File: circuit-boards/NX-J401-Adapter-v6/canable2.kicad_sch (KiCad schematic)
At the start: 26 parts, among them J8 SWD, J9 CFG, Q6 SI2301CDS-T1-GE3, Q7 SS8050, Q8 SI2301CDS-T1-GE3, U2 RT9013-33GB, U3 STM32G431CBTx, U4 TJA1051TK-3

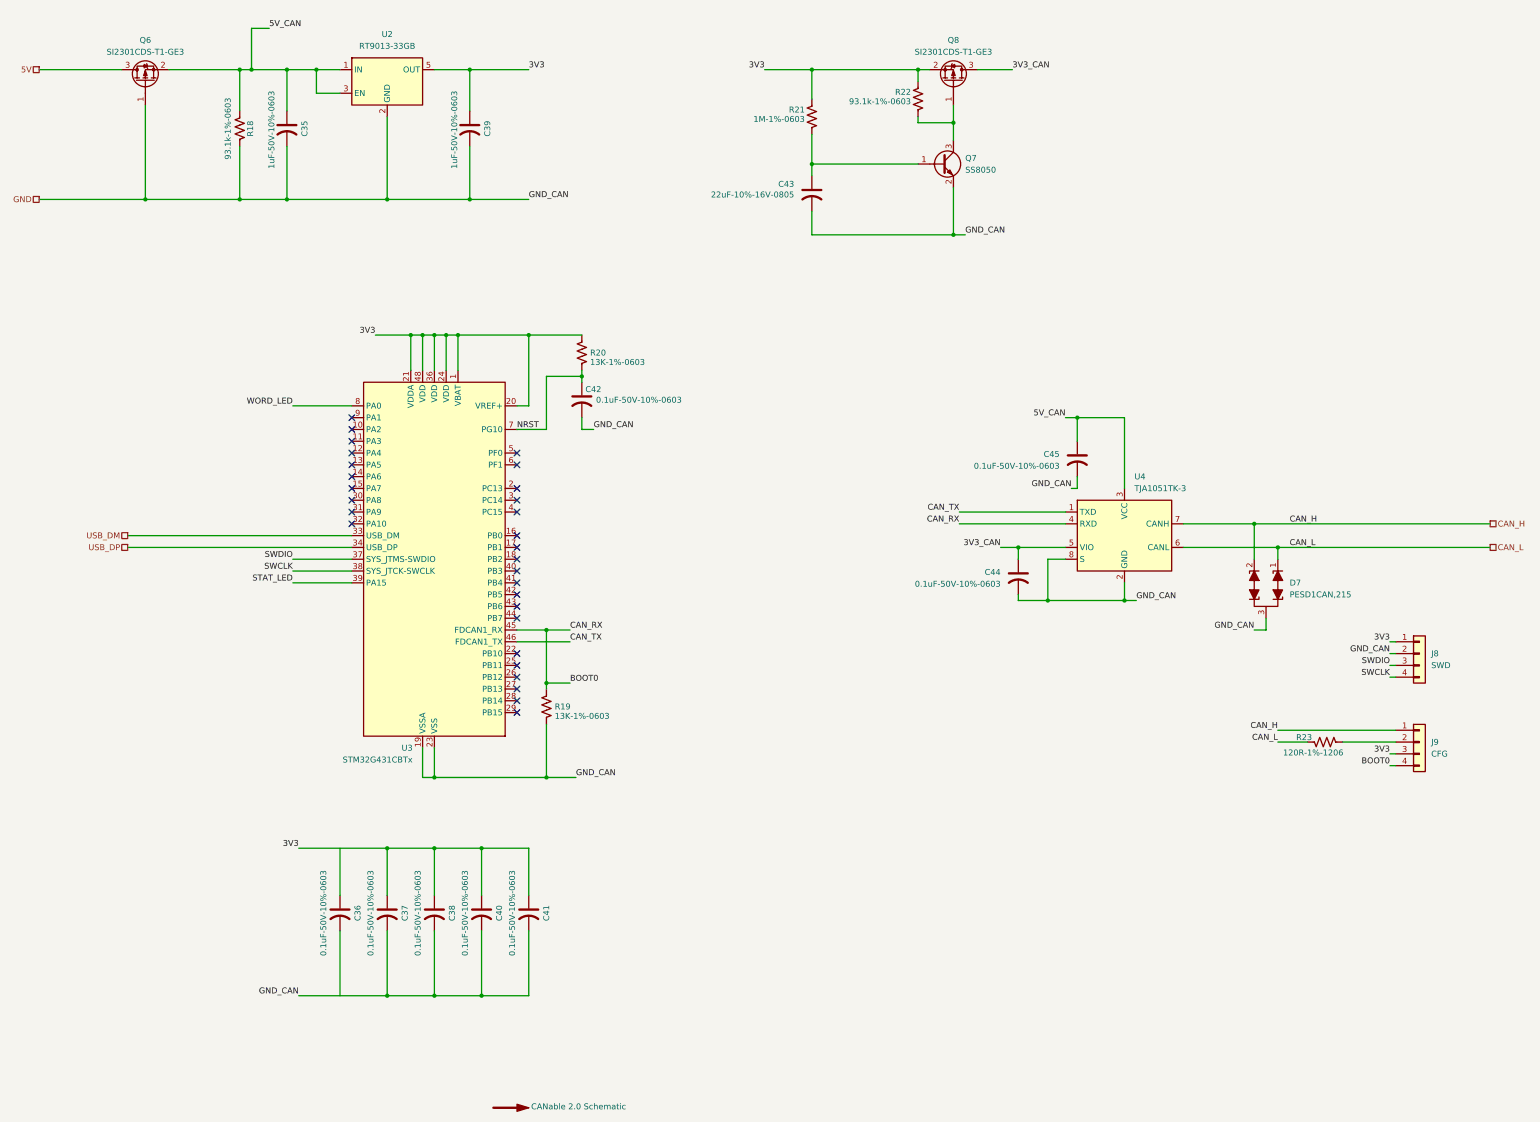
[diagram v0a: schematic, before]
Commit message: Changed canable to use 3.3V power form USB to use key-e connector that breaks out USB and 3V3
Signed-off-by: Scott Berman <sgberman1@gmail.com>
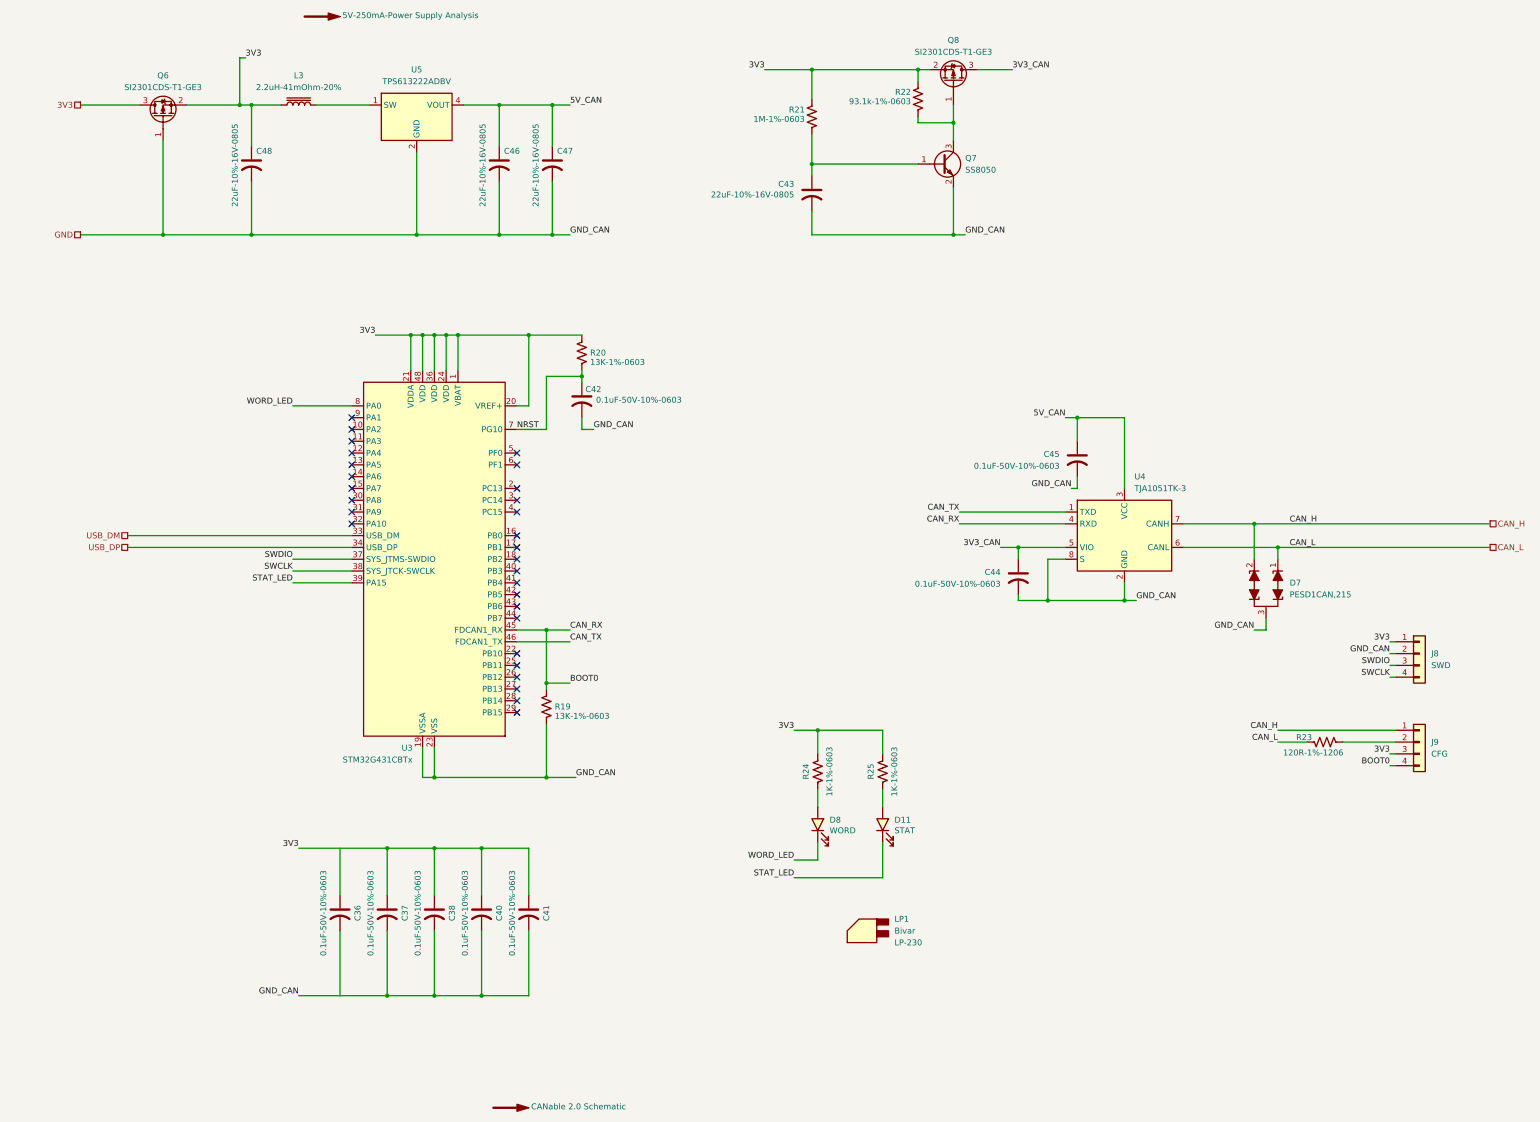
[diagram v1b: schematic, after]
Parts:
- removed C35, C39: 1uF-50V-10%-0603, Capacitor_SMD:C_0603_1608Metric, symbol Device:C_US
- removed R18: 93.1k-1%-0603, Resistor_SMD:R_0603_1608Metric, symbol Device:R_US
- removed U2: RT9013-33GB, Package_TO_SOT_SMD:SOT-23-5, symbol NX-J401-Adapter:RT9013-33GB
- added C46, C47, C48: 22uF-10%-16V-0805, Capacitor_SMD:C_0805_2012Metric, symbol Device:C_US
- added D11: STAT, LED_SMD:LED_1206_3216Metric, symbol Device:LED
- added D8: WORD, LED_SMD:LED_1206_3216Metric, symbol Device:LED
- added L3: 2.2uH-41mOhm-20%, NX-J401-Adapter:KOHER-MDA4020-2R2M, symbol Device:L_Iron
- added LP1: (no value), NX-J401-Adapter:Bivar-LP-230, symbol NX-J401-Adapter:Light_Pipe
- added R24, R25: 1K-1%-0603, Resistor_SMD:R_0603_1608Metric, symbol Device:R_US
- added U5: TPS613222ADBV, Package_TO_SOT_SMD:SOT-23-5, symbol Regulator_Switching:TPS613222ADBV
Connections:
- net 5V is gone; now on net 3V3: Q6.3 (D)
- net 3V3: now also Q6.2 (S), C48.1, L3.1, R24.1, R25.1
- net 5V_CAN: now also C46.1, C47.1, U5.4 (VOUT); no longer Q6.2 (S)
- net GND: now also C46.2, C47.2, C48.2, U5.2 (GND)
- net STAT_LED: now also D11.1 (K)
- net WORD_LED: now also D8.1 (K)
- new net: D11.2 (A), R25.2
- new net: D8.2 (A), R24.2
- new net: L3.2, U5.1 (SW)
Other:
- moved on the sheet: Q6

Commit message: WIP update
Signed-off-by: Scott Berman <sgberman1@gmail.com>
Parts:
- J8: footprint Connector_PinHeader_2.54mm:PinHeader_1x04_P2.54mm_Vertical -> Connector_PinHeader_2.54mm:PinHeader_1x04_P2.54mm_Horizontal
- J9: footprint Connector_PinHeader_2.54mm:PinHeader_2x02_P2.54mm_Vertical -> Connector_PinHeader_2.54mm:PinHeader_1x04_P2.54mm_Horizontal
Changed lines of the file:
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@@
 			)
 		)
-		(property "Footprint" "Connector_PinHeader_2.54mm:PinHeader_2x02_P2.54mm_Vertical"
+		(property "Footprint" "Connector_PinHeader_2.54mm:PinHeader_1x04_P2.54mm_Horizontal"
 			(at 346.71 177.8 0)
 			(hide yes)
@@
 			)
 		)
-		(property "Footprint" "Connector_PinHeader_2.54mm:PinHeader_1x04_P2.54mm_Vertical"
+		(property "Footprint" "Connector_PinHeader_2.54mm:PinHeader_1x04_P2.54mm_Horizontal"
 			(at 346.71 158.75 0)
 			(hide yes)

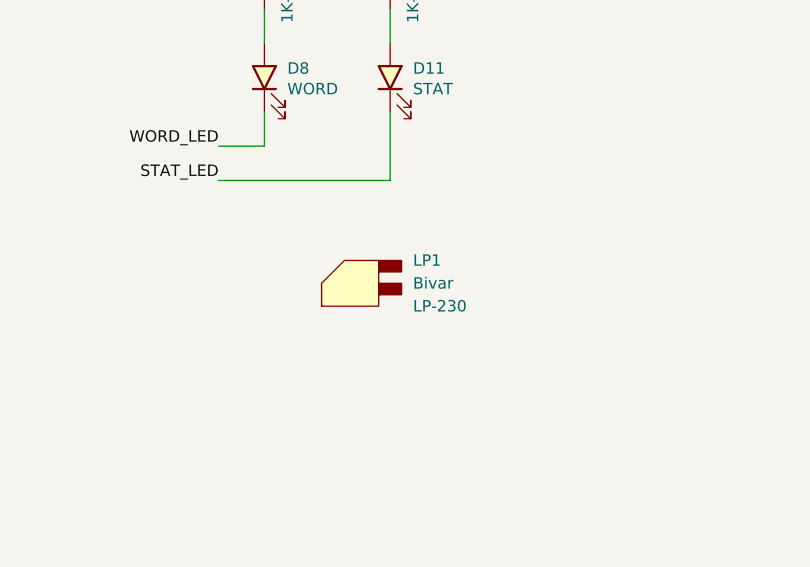
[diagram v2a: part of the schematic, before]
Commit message: Changed USB header ot pico lock and light pipe to single row
Signed-off-by: Scott Berman <sgberman1@gmail.com>
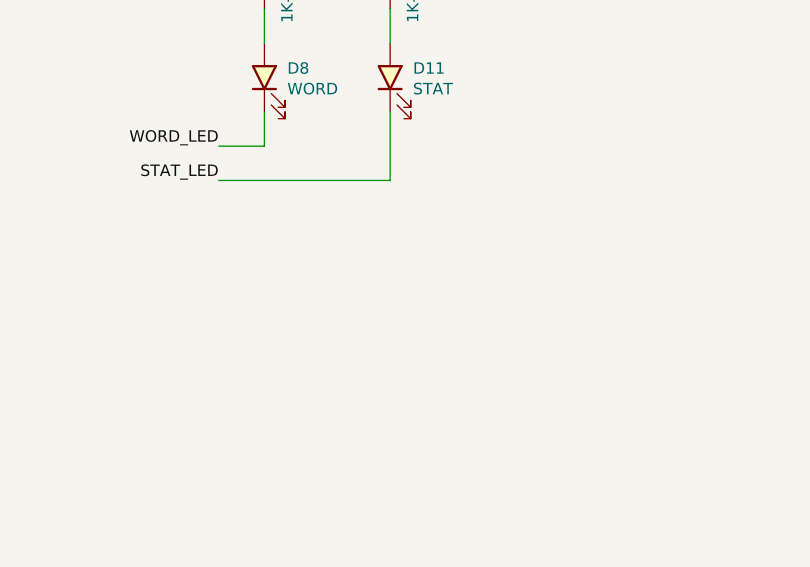
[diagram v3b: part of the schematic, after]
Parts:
- removed LP1: (no value), NX-J401-Adapter:Bivar-LP-230, symbol NX-J401-Adapter:Light_Pipe
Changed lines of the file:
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@@
-	)
-	(symbol
-		(lib_id "NX-J401-Adapter:Light_Pipe")
-		(at 223.52 218.44 0)
-		(unit 1)
-		(body_style 1)
-		(exclude_from_sim no)
-		(in_bom yes)
-		(on_board yes)
-		(in_pos_files yes)
-		(dnp no)
-		(fields_autoplaced yes)
-		(property "Reference" "LP1"
-			(at 233.68 215.8999 0)
-			(show_name no)
-			(do_not_autoplace no)
-			(effects
-				(font
-					(size 1.27 1.27)
-				)
-				(justify left)
-			)
-		)
-		(property "Value" ""
-			(at 223.52 218.44 0)
-			(show_name no)
-			(do_not_autoplace no)
-			(effects
-				(font
-					(size 1.27 1.27)
-				)
-			)
-		)
-		(property "Footprint" "NX-J401-Adapter:Bivar-LP-230"
-			(at 223.52 218.44 0)
-			(hide yes)
-			(show_name no)
-			(do_not_autoplace no)
-			(effects
-				(font
-					(size 1.27 1.27)
-				)
-			)
-		)
-		(property "Datasheet" "Components/Bivar-LP-230.pdf"
-			(at 223.52 218.44 0)
-			(hide yes)
-			(show_name no)
-			(do_not_autoplace no)
-			(effects
-				(font
-					(size 1.27 1.27)
-				)
-			)
-		)
-		(property "Description" ""
-			(at 223.52 218.44 0)
-			(hide yes)
-			(show_name no)
-			(do_not_autoplace no)
-			(effects
-				(font
-					(size 1.27 1.27)
-				)
-			)
-		)
-		(property "MFG" "Bivar"
-			(at 233.68 218.4399 0)
-			(show_name no)
-			(do_not_autoplace no)
-			(effects
-				(font
-					(size 1.27 1.27)
-				)
-				(justify left)
-			)
-		)
-		(property "MFG P/N" "LP-230"
-			(at 233.68 220.9799 0)
-			(show_name no)
-			(do_not_autoplace no)
-			(effects
-				(font
-					(size 1.27 1.27)
-				)
-				(justify left)
-			)
-		)
-		(property "DIST" "Digikey"
-			(at 223.52 218.44 0)
-			(hide yes)
-			(show_name no)
-			(do_not_autoplace no)
-			(effects
-				(font
-					(size 1.27 1.27)
-				)
-			)
-		)
-		(property "DIST P/N" "492-1859-ND"
-			(at 223.52 218.44 0)
-			(hide yes)
-			(show_name no)
-			(do_not_autoplace no)
-			(effects
-				(font
-					(size 1.27 1.27)
-				)
-			)
-		)
-		(instances
-			(project "NX-J401-Adapter-v6"
-				(path "/3c9fa76f-2b37-4666-8575-58caa65def04/958ef65b-dc3d-4755-b7b0-3d4dc8feed9f"
-					(reference "LP1")
-					(unit 1)
-				)
-			)
-		)
 	)
 	(symbol

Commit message: Improved placement.  Pre-routing
Signed-off-by: Scott Berman <sgberman1@gmail.com>
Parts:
- removed J8: SWD, Connector_PinHeader_2.54mm:PinHeader_1x04_P2.54mm_Horizontal, symbol Connector_Generic:Conn_01x04
- removed J9: CFG, Connector_PinHeader_2.54mm:PinHeader_1x04_P2.54mm_Horizontal, symbol Connector_Generic:Conn_01x04
- removed R23: 120R-1%-1206, Resistor_SMD:R_1206_3216Metric, symbol Device:R_US
- added J1: SWD, Connector_PinHeader_2.54mm:PinHeader_1x05_P2.54mm_Horizontal, symbol Connector_Generic:Conn_01x05
- U4: value TJA1051TK-3 -> TJA1051T/3/1J; footprint Package_SON:HVSON-8-1EP_3x3mm_P0.65mm_EP1.6x2.4mm -> Package_SO:SO-8_3.9x4.9mm_P1.27mm
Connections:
- net 3V3: now also C36.1, J1.2 (Pin_2); no longer Q6.3 (D)
- net BOOT0: now also J1.1 (Pin_1)
- net SWCLK: now also J1.5 (Pin_5)
- net SWDIO: now also J1.4 (Pin_4)
- net GND_CAN: now reaches C36.2
- net GND_CAN: now also C37.2, C38.2, C40.2, C41.2, C42.2, C43.2, C44.2, C45.2, C46.2, C47.2, C48.2, D7.3 (KK), Q6.1 (G), Q7.2 (E), R19.2, U3.19 (VSSA), U3.23 (VSS), U3.35 (VSS), U3.47 (VSS), U4.2 (GND), U4.8 (S), U5.2 (GND), J1.3 (Pin_3)
- removed net GND: C37.2, C38.2, C40.2, C41.2, C42.2, C43.2, C44.2, C45.2, C46.2, C47.2, C48.2, D7.3 (KK), Q6.1 (G), Q7.2 (E), R19.2, U3.19 (VSSA), U3.23 (VSS), U3.35 (VSS), U3.47 (VSS), U4.2 (GND), U4.8 (S), U4.9 (GND), U5.2 (GND)
- new net 3V3_USB: Q6.3 (D)

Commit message: Initial fully routed PCB
Signed-off-by: Scott Berman <sgberman1@gmail.com>
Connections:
- net 3V3: now also D11.2 (A), D8.2 (A); no longer R24.1, R25.1
- net STAT_LED: now also R25.2; no longer D11.1 (K)
- net WORD_LED: now also R24.2; no longer D8.1 (K)
- new net: D11.1 (K), R25.1
- new net: D8.1 (K), R24.1
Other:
- moved on the sheet: D11, D8, R24, R25

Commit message: Initial complete routing
Signed-off-by: Scott Berman <sgberman1@gmail.com>
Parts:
- C1: renamed from C47; KiLib_Generator (none) -> SMD_2terminal_chip_molded
- C11: renamed from C40; KiLib_Generator (none) -> SMD_2terminal_chip_molded
- C2: renamed from C46; KiLib_Generator (none) -> SMD_2terminal_chip_molded
- C21: renamed from C42; KiLib_Generator (none) -> SMD_2terminal_chip_molded
- C22: renamed from C43; KiLib_Generator (none) -> SMD_2terminal_chip_molded
- C3: renamed from C48; KiLib_Generator (none) -> SMD_2terminal_chip_molded
- C36: renamed from C45; KiLib_Generator (none) -> SMD_2terminal_chip_molded
- C44: KiLib_Generator (none) -> SMD_2terminal_chip_molded
- C6: renamed from C41; KiLib_Generator (none) -> SMD_2terminal_chip_molded
- C7: renamed from C37; KiLib_Generator (none) -> SMD_2terminal_chip_molded
- C8: renamed from C38; KiLib_Generator (none) -> SMD_2terminal_chip_molded
- C9: renamed from C36; KiLib_Generator (none) -> SMD_2terminal_chip_molded
- D5: renamed from D7; KiLib_Generator (none) -> package/gullwing
- D8: renamed from D11; KiLib_Generator (none) -> SMD_2terminal_chip_molded
- D9: renamed from D8; KiLib_Generator (none) -> SMD_2terminal_chip_molded
- J8: renamed from J1; DIST (none) -> Digikey; DIST P/N (none) -> 2057-PH1RB-05-UA-ND; KiLib_Generator (none) -> connector/pin_header_socket; MFG (none) -> Adam Tech; MFG P/N (none) -> PH1RB-05-UA
- Q1: renamed from Q6; KiLib_Generator (none) -> package/gullwing
- Q5: renamed from Q7; KiLib_Generator (none) -> package/gullwing
- Q8, U3: KiLib_Generator (none) -> package/gullwing
- R1: renamed from R19; KiLib_Generator (none) -> SMD_2terminal_chip_molded
- R2: renamed from R20; KiLib_Generator (none) -> SMD_2terminal_chip_molded
- R3: renamed from R24; KiLib_Generator (none) -> SMD_2terminal_chip_molded
- R4: renamed from R25; KiLib_Generator (none) -> SMD_2terminal_chip_molded
- R5: renamed from R22; KiLib_Generator (none) -> SMD_2terminal_chip_molded
- R7: renamed from R21; KiLib_Generator (none) -> SMD_2terminal_chip_molded
- U1: renamed from U5; KiLib_Generator (none) -> package/gullwing
- U6: renamed from U4; KiLib_Generator (none) -> package/gullwing
- renumbered L3 to L1

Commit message: Moved the Vout connector to increase clearance
Signed-off-by: Scott Berman <sgberman1@gmail.com>
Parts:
- D8, D9: DIST Digikey -> (none); DIST P/N 1080-1418-1-ND -> (none); JLCPCB P/N (none) -> C965824; MFG Everlight -> XINGLIGHT; MFG P/N QTLP650D3TR -> XL-3216UYC
- J8: JLCPCB P/N (none) -> XXXXXX
- U1: DIST (none) -> Digikey; DIST P/N (none) -> 296-50503-1-ND; JLCPCB P/N (none) -> C2071163; MFG (none) -> Texas Instruments; MFG P/N (none) -> TPS613222ADBVR
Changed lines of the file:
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@@
 			)
 		)
-		(property "Datasheet" ""
+		(property "Datasheet" "Components/Adam-Tech-ph1rb-xx-ua.pdf"
 			(at 317.5 173.99 0)
 			(hide yes)
@@
 			)
 		)
+		(property "JLCPCB P/N" "XXXXXX"
+			(at 317.5 173.99 0)
+			(hide yes)
+			(show_name no)
+			(do_not_autoplace no)
+			(effects
+				(font
+					(size 1.27 1.27)
+				)
+			)
+		)
 		(pin "2"
 		)
@@
 			)
 		)
-		(property "Datasheet" "Components/Everlight-QTLP650(C,D)-2,3,4,7,B.pdf"
+		(property "Datasheet" ""
 			(at 231.14 182.88 0)
 			(hide yes)
@@
 			)
 		)
-		(property "DIST" "Digikey"
+		(property "DIST" ""
 			(at 231.14 182.88 0)
 			(hide yes)
@@
 			)
 		)
-		(property "DIST P/N" "1080-1418-1-ND"
+		(property "DIST P/N" ""
 			(at 231.14 182.88 0)
 			(hide yes)
@@
 			)
 		)
-		(property "MFG" "Everlight"
+		(property "MFG" "XINGLIGHT"
 			(at 231.14 182.88 0)
 			(hide yes)
@@
 			)
 		)
-		(property "MFG P/N" "QTLP650D3TR"
+		(property "MFG P/N" "XL-3216UYC "
 			(at 231.14 182.88 0)
 			(hide yes)
@@
 			)
 		)
+		(property "JLCPCB P/N" "C965824"
+			(at 231.14 182.88 90)
+			(hide yes)
+			(show_name no)
+			(do_not_autoplace no)
+			(effects
+				(font
+					(size 1.27 1.27)
+				)
+			)
+		)
 		(pin "1"
 		)
@@
 			)
 		)
-		(property "Datasheet" "Components/Everlight-QTLP650(C,D)-2,3,4,7,B.pdf"
+		(property "Datasheet" ""
 			(at 217.17 182.88 0)
 			(hide yes)
@@
 			)
 		)
-		(property "DIST" "Digikey"
+		(property "DIST" ""
 			(at 217.17 182.88 0)
 			(hide yes)
@@
 			)
 		)
-		(property "DIST P/N" "1080-1418-1-ND"
+		(property "DIST P/N" ""
 			(at 217.17 182.88 0)
 			(hide yes)
@@
 			)
 		)
-		(property "MFG" "Everlight"
+		(property "MFG" "XINGLIGHT"
 			(at 217.17 182.88 0)
 			(hide yes)
@@
 			)
 		)
-		(property "MFG P/N" "QTLP650D3TR"
+		(property "MFG P/N" "XL-3216UYC "
 			(at 217.17 182.88 0)
 			(hide yes)
@@
 			)
 		)
+		(property "JLCPCB P/N" "C965824"
+			(at 217.17 182.88 90)
+			(hide yes)
+			(show_name no)
+			(do_not_autoplace no)
+			(effects
+				(font
+					(size 1.27 1.27)
+				)
+			)
+		)
 		(pin "1"
 		)
@@
 			(at 130.81 43.18 0)
 			(hide yes)
+			(show_name no)
+			(do_not_autoplace no)
+			(effects
+				(font
+					(size 1.27 1.27)
+				)
+			)
+		)
+		(property "MFG" "Texas Instruments"
+			(at 130.81 43.18 0)
+			(hide yes)
+			(show_name no)
+			(do_not_autoplace no)
+			(effects
+				(font
+					(size 1.27 1.27)
+				)
+			)
+		)
+		(property "MFG P/N" "TPS613222ADBVR"
+			(at 130.81 43.18 0)
+			(hide yes)
+			(show_name no)
+			(do_not_autoplace no)
+			(effects
+				(font
+					(size 1.27 1.27)
+				)
+			)
+		)
+		(property "DIST" "Digikey"
+			(at 130.81 43.18 0)
+			(hide yes)
+			(show_name no)
+			(do_not_autoplace no)
+			(effects
+				(font
+					(size 1.27 1.27)
+				)
+			)
+		)
+		(property "DIST P/N" "296-50503-1-ND"
+			(at 130.81 43.18 0)
+			(hide yes)
+			(show_name no)
+			(do_not_autoplace no)
+			(effects
+				(font
+					(size 1.27 1.27)
+				)
+			)
+		)
+		(property "JLCPCB P/N" "C2071163"
+			(at 130.81 43.18 0)
+			(hide yes)

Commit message: minor fixes
Signed-off-by: Scott Berman <sgberman1@gmail.com>
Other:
- company: (none) -> SPACE COOKIES FRC TEAM 1868
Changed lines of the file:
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@@
 	(title_block
 		(title "NX J401 Adapter")
-		(date "2026-05-10")
+		(date "2026-05-25")
 		(rev "6")
+		(company "SPACE COOKIES FRC TEAM 1868")
 	)
 	(junction
